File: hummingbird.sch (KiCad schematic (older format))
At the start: 40 parts

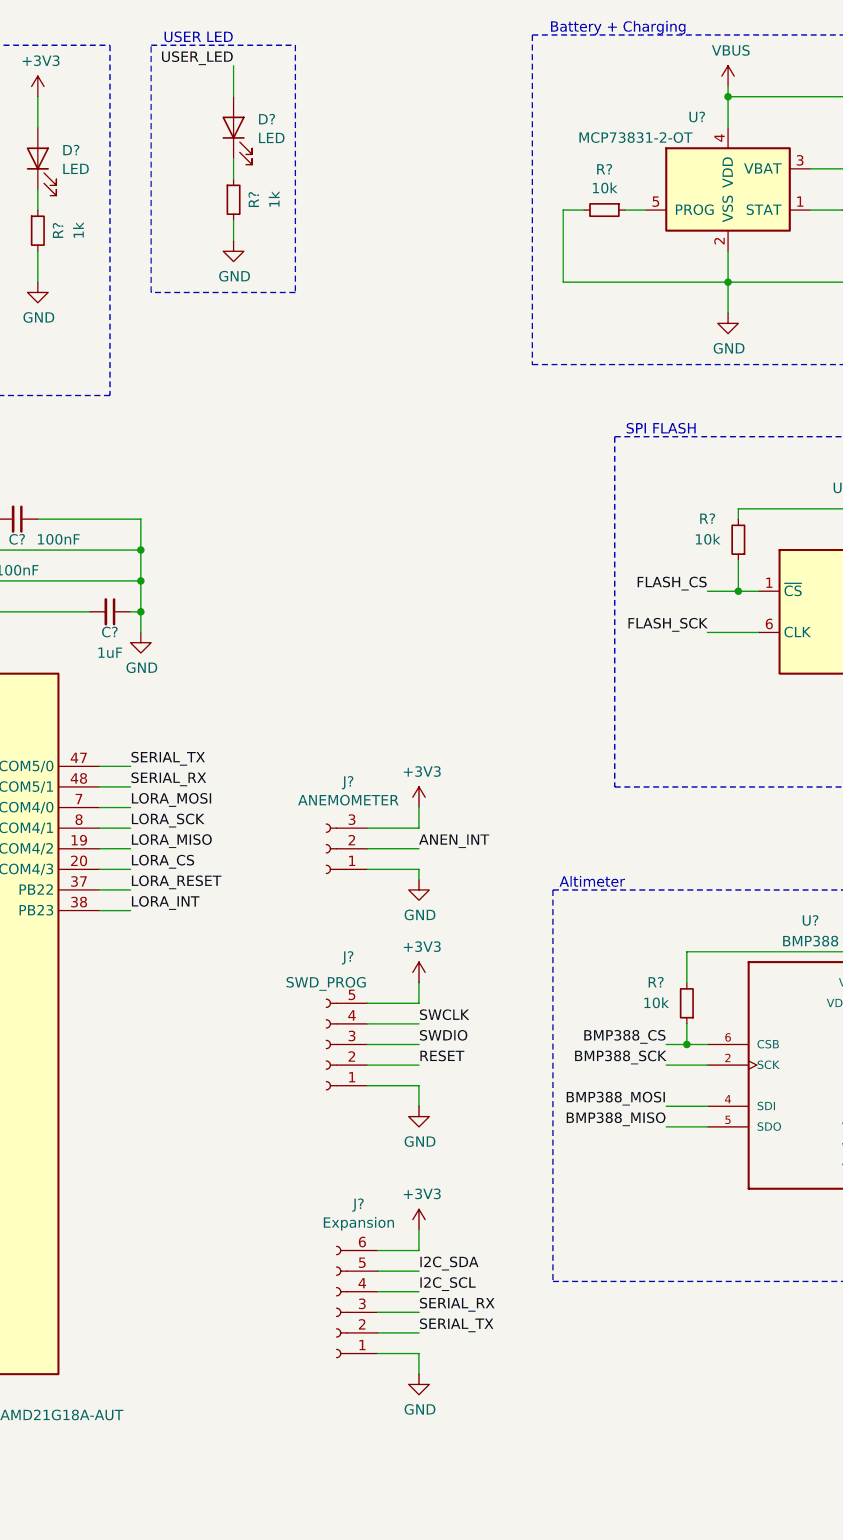
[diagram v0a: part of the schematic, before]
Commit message: renaming things, add SOIC prog clip header
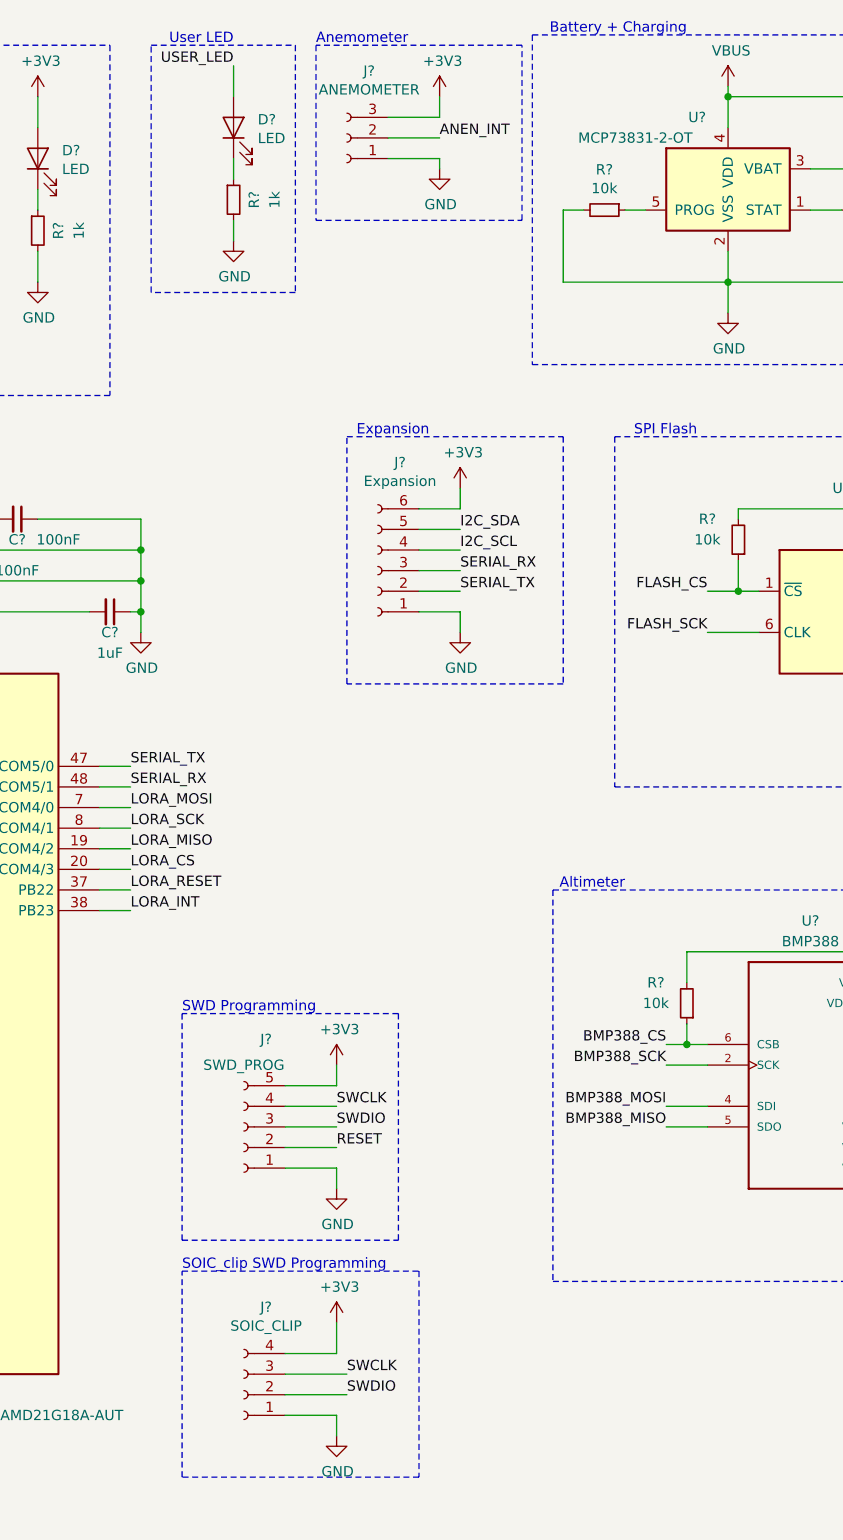
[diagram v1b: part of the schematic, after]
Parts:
- added J?: SOIC_CLIP, symbol Connector:Conn_01x04_Female
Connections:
- net +3V3: now also J?.4 (Pin_4)
- net GND: now also J?.1 (Pin_1)
- net SWCLK: now also J?.3 (Pin_3)
- net SWDIO: now also J?.2 (Pin_2)
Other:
- note added: "Anemometer"
- note added: "Expansion"
- note added: "SOIC_clip SWD Programming"
- note added: "SPI Flash"
- note added: "SWD Programming"
- note added: "User LED"
- note removed: "SPI FLASH"
- note removed: "USER LED"
- moved on the sheet: J?

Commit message: schematic first draft
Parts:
- added TP?: XOUT32, symbol Connector:TestPoint
- added TP?: XIN32, symbol Connector:TestPoint
- C?: value ?? -> 1uF
- J?: value JSTPH -> JST
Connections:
- net at C?.2, U?.1 (PA00), Y?.2: now also TP?.1
- net at C?.2, U?.2 (PA01), Y?.1: now also TP?.1
- no-connect marks 13 -> 21
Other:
- note added: "MCU"
- note removed: "todo"
- moved on the sheet: C?, D?, J?, R?, U?, Y?

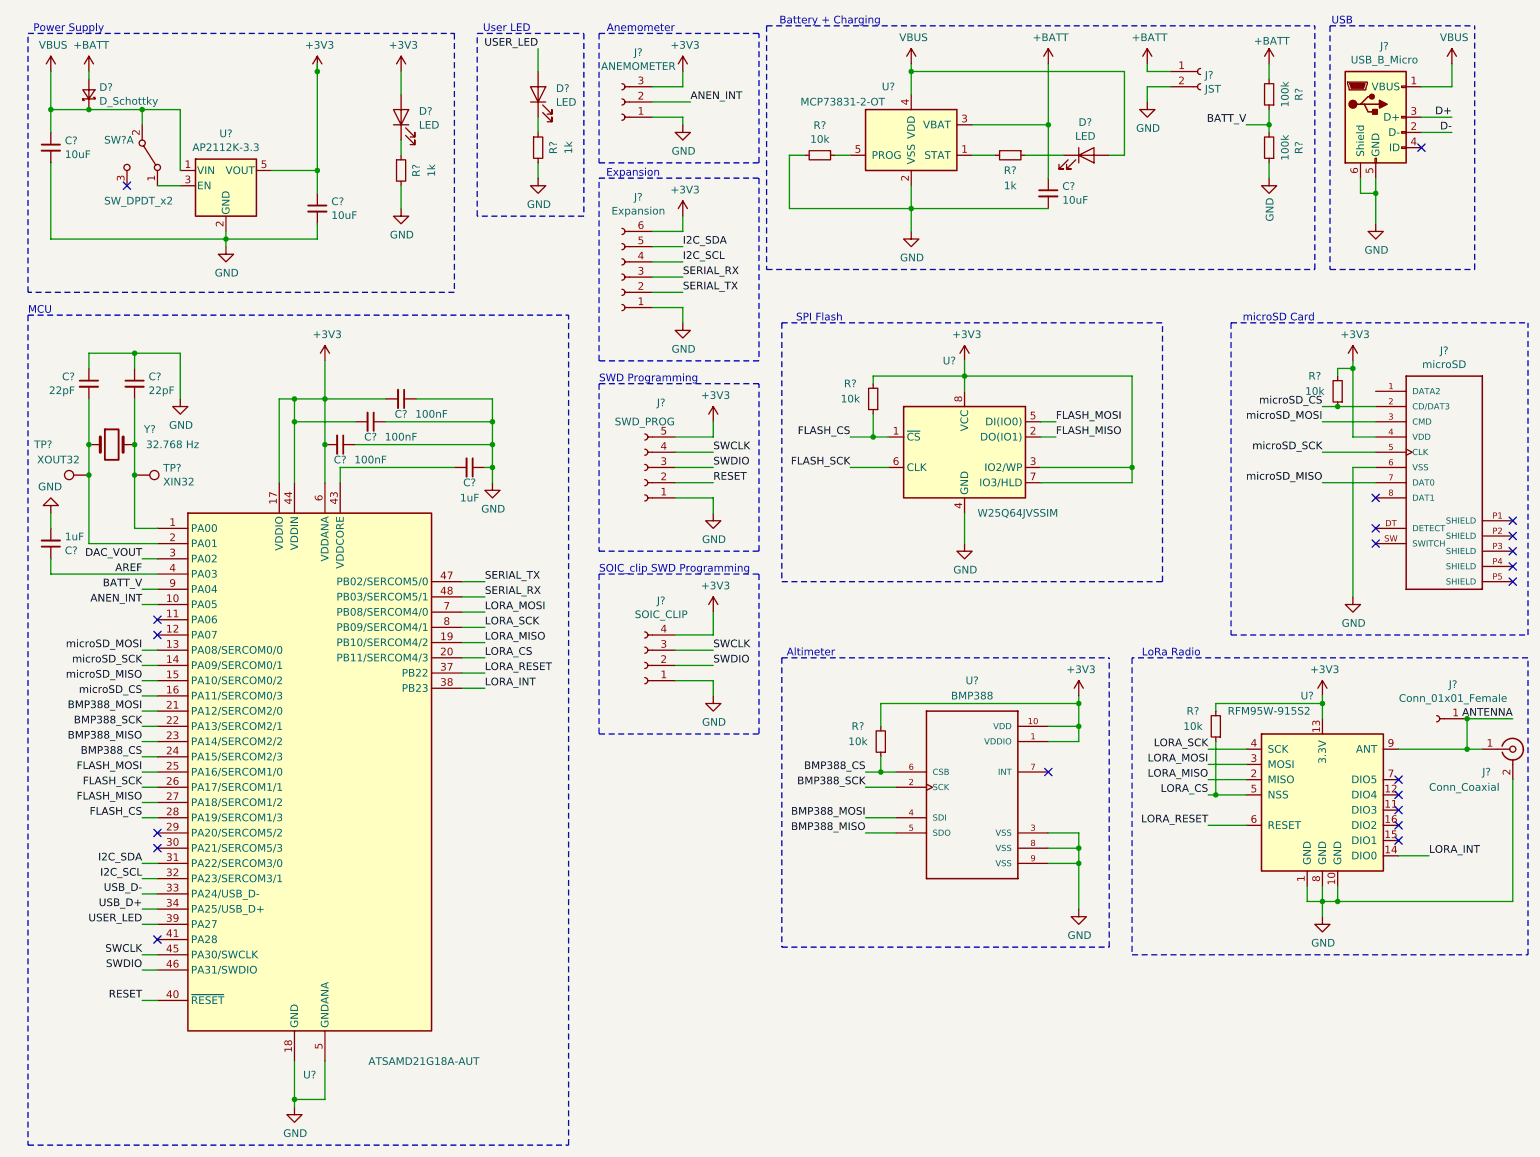
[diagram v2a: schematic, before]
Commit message: actually finish schematic and connect pins
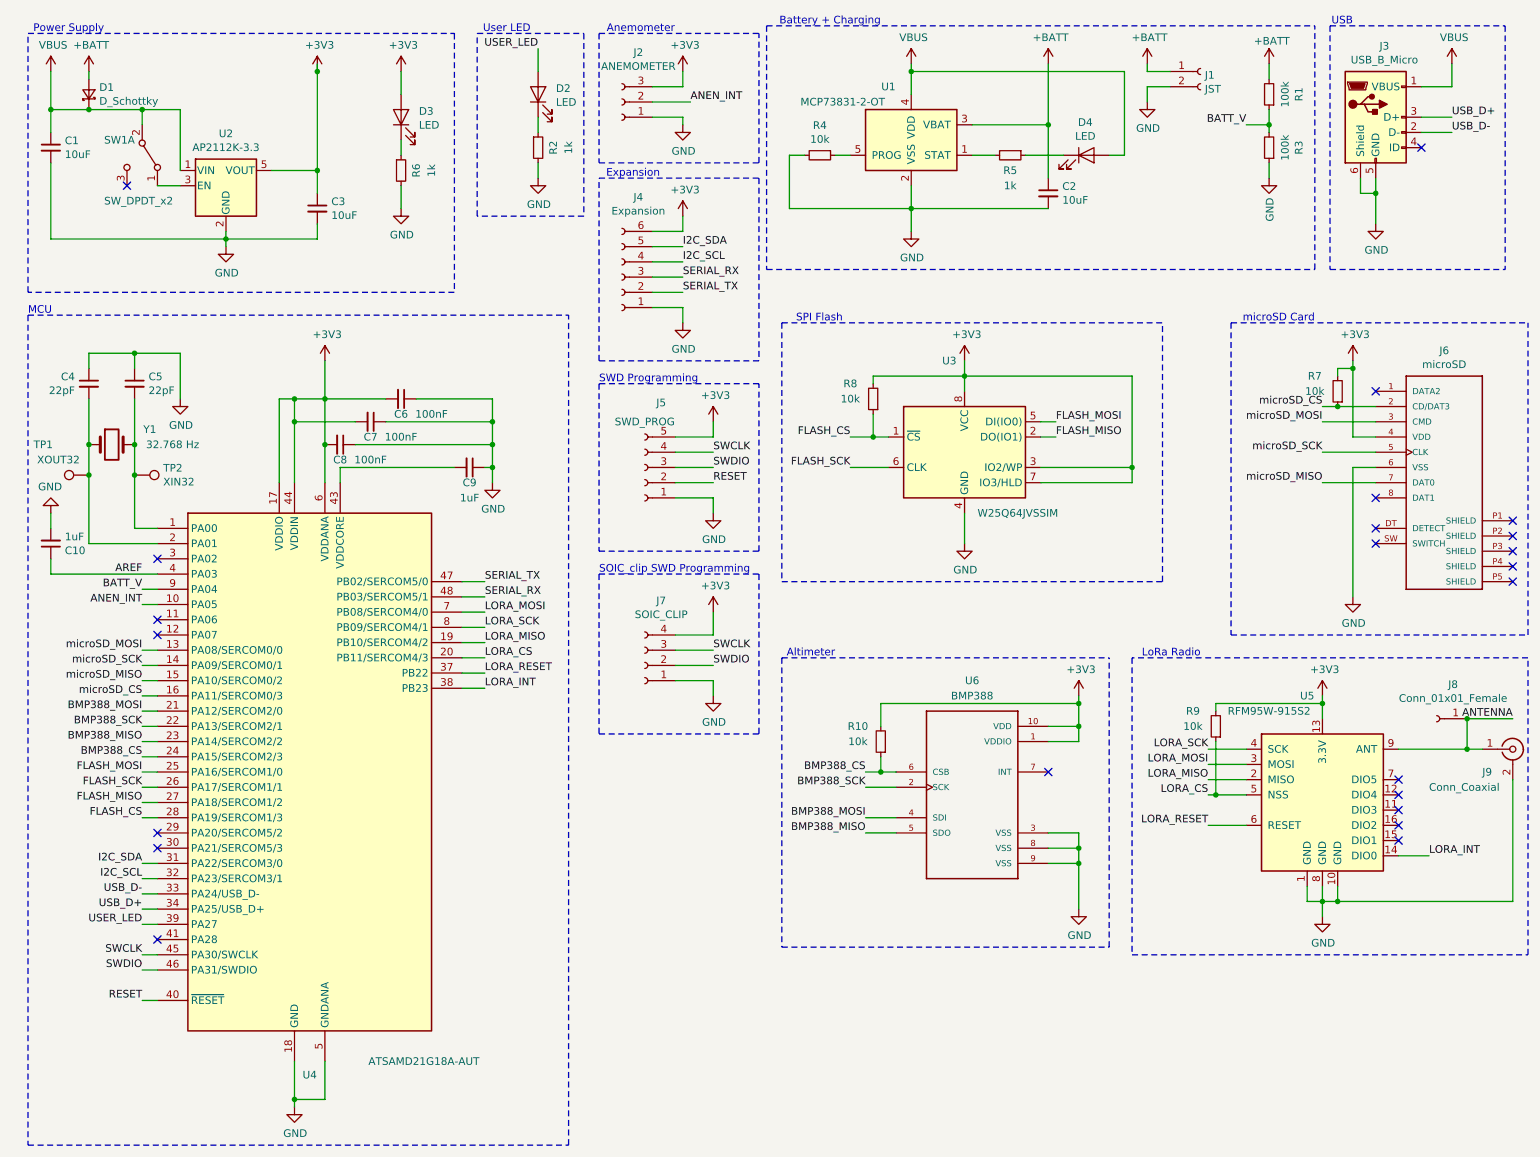
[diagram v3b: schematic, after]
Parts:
- gave numbers to parts that had none: 43
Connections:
- net D+ is gone; now on net USB_D+: J3.3 (D+)
- net D- is gone; now on net USB_D-: J3.2 (D-)
- net DAC_VOUT: no longer names the net of U4.3 (PA02)
- no-connect marks 21 -> 23

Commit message: start adding footprints
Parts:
- C1, C10, C2, C3, C4, C5, C6, C7, C8, C9: footprint (none) -> Capacitor_SMD:C_0603_1608Metric
- D1: footprint (none) -> Diode_SMD:D_0603_1608Metric
- D2, D3, D4: footprint (none) -> LED_SMD:LED_0603_1608Metric
- J2: footprint (none) -> Connector_PinHeader_2.54mm:PinHeader_1x03_P2.54mm_Vertical
- J4: footprint (none) -> Connector_PinHeader_2.54mm:PinHeader_1x06_P2.54mm_Vertical
- J5: footprint (none) -> Connector_PinHeader_2.54mm:PinHeader_1x05_P2.54mm_Vertical
- J6: footprint MOLEX_503182-1852 -> (none)
- J9: footprint (none) -> Connector_Coaxial:SMA_Molex_73251-1153_EdgeMount_Horizontal
- R1, R10, R2, R3, R4, R5, R6, R7, R8, R9: footprint (none) -> Resistor_SMD:R_0603_1608Metric
- TP1, TP2: footprint (none) -> TestPoint:TestPoint_Pad_D1.0mm
- U6: footprint PQFN50P200X200X80-10N -> (none)
- Y1: footprint (none) -> Crystal:Crystal_SMD_3215-2Pin_3.2x1.5mm
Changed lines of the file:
@@
 F 0 "C9" V 3600 3500 50  0000 C CNN
 F 1 "1uF" V 3700 3500 50  0000 C CNN
-F 2 "" H 3500 3500 50  0001 C CNN
+F 2 "Capacitor_SMD:C_0603_1608Metric" H 3500 3500 50  0001 C CNN
 F 3 "~" H 3500 3500 50  0001 C CNN
 	1    3500 3500
@@
 F 0 "C8" V 2750 3350 50  0000 C CNN
 F 1 "100nF" V 2750 3550 50  0000 C CNN
-F 2 "" H 2650 3350 50  0001 C CNN
+F 2 "Capacitor_SMD:C_0603_1608Metric" H 2650 3350 50  0001 C CNN
 F 3 "~" H 2650 3350 50  0001 C CNN
 	1    2650 3350
@@
 F 0 "C7" V 2950 3200 50  0000 C CNN
 F 1 "100nF" V 2950 3400 50  0000 C CNN
-F 2 "" H 2850 3200 50  0001 C CNN
+F 2 "Capacitor_SMD:C_0603_1608Metric" H 2850 3200 50  0001 C CNN
 F 3 "~" H 2850 3200 50  0001 C CNN
 	1    2850 3200
@@
 F 0 "C6" V 3150 3050 50  0000 C CNN
 F 1 "100nF" V 3150 3250 50  0000 C CNN
-F 2 "" H 3050 3050 50  0001 C CNN
+F 2 "Capacitor_SMD:C_0603_1608Metric" H 3050 3050 50  0001 C CNN
 F 3 "~" H 3050 3050 50  0001 C CNN
 	1    3050 3050
@@
 F 0 "C3" H 2592 1846 50  0000 L CNN
 F 1 "10uF" H 2592 1755 50  0000 L CNN
-F 2 "" H 2500 1800 50  0001 C CNN
+F 2 "Capacitor_SMD:C_0603_1608Metric" H 2500 1800 50  0001 C CNN
 F 3 "~" H 2500 1800 50  0001 C CNN
 	1    2500 1800
@@
 F 0 "D1" V 1046 982 50  0000 R CNN
 F 1 "D_Schottky" V 955 982 50  0000 R CNN
-F 2 "" V 1000 1050 50  0001 C CNN
+F 2 "Diode_SMD:D_0603_1608Metric" V 1000 1050 50  0001 C CNN
 F 3 "~" V 1000 1050 50  0001 C CNN
 	1    1000 1050
@@
 F 0 "C1" H 842 1446 50  0000 L CNN
 F 1 "10uF" H 842 1355 50  0000 L CNN
-F 2 "" H 750 1400 50  0001 C CNN
+F 2 "Capacitor_SMD:C_0603_1608Metric" H 750 1400 50  0001 C CNN
 F 3 "~" H 750 1400 50  0001 C CNN
 	1    750  1400
@@
 F 0 "D4" H 7543 1666 50  0000 C CNN
 F 1 "LED" H 7543 1575 50  0000 C CNN
-F 2 "" H 7550 1450 50  0001 C CNN
+F 2 "LED_SMD:LED_0603_1608Metric" H 7550 1450 50  0001 C CNN
 F 3 "~" H 7550 1450 50  0001 C CNN
 	1    7550 1450
@@
 F 0 "R5" V 7150 1450 50  0000 C CNN
 F 1 "1k" V 7250 1450 50  0000 C CNN
-F 2 "" H 7050 1450 50  0001 C CNN
+F 2 "Resistor_SMD:R_0603_1608Metric" H 7050 1450 50  0001 C CNN
 F 3 "~" H 7050 1450 50  0001 C CNN
 	1    7050 1450
@@
 F 0 "C2" H 7392 1746 50  0000 L CNN
 F 1 "10uF" H 7392 1655 50  0000 L CNN
-F 2 "" H 7300 1700 50  0001 C CNN
+F 2 "Capacitor_SMD:C_0603_1608Metric" H 7300 1700 50  0001 C CNN
 F 3 "~" H 7300 1700 50  0001 C CNN
 	1    7300 1700
@@
 F 0 "R4" V 5604 1450 50  0000 C CNN
 F 1 "10k" V 5695 1450 50  0000 C CNN
-F 2 "" H 5800 1450 50  0001 C CNN
+F 2 "Resistor_SMD:R_0603_1608Metric" H 5800 1450 50  0001 C CNN
 F 3 "~" H 5800 1450 50  0001 C CNN
 	1    5800 1450
@@
 F 0 "R1" V 8554 1050 50  0000 C CNN
 F 1 "100k" V 8645 1050 50  0000 C CNN
-F 2 "" H 8750 1050 50  0001 C CNN
+F 2 "Resistor_SMD:R_0603_1608Metric" H 8750 1050 50  0001 C CNN
 F 3 "~" H 8750 1050 50  0001 C CNN
 	1    8750 1050
@@
 F 0 "R3" V 8554 1400 50  0000 C CNN
 F 1 "100k" V 8645 1400 50  0000 C CNN
-F 2 "" H 8750 1400 50  0001 C CNN
+F 2 "Resistor_SMD:R_0603_1608Metric" H 8750 1400 50  0001 C CNN
 F 3 "~" H 8750 1400 50  0001 C CNN
 	1    8750 1400
@@
 F 0 "U6" H 6800 6500 50  0000 C CNN
 F 1 "BMP388" H 6800 6400 50  0000 C CNN
-F 2 "PQFN50P200X200X80-10N" H 6800 5700 50  0001 L BNN
+F 2 "" H 6800 5700 50  0001 L BNN
 F 3 "https://ae-bst.resource.bosch.com/media/_tech/media/datasheets/BST-BMP388-DS001.pdf" H 6800 5700 50  0001 L BNN
 F 4 "828-1079-1-ND" H 6800 5700 50  0001 L BNN "Field4"
@@
 F 0 "J6" H 9900 4467 50  0000 C CNN
 F 1 "microSD" H 9900 4376 50  0000 C CNN
-F 2 "MOLEX_503182-1852" H 10400 3400 50  0001 L BNN
+F 2 "" H 10400 3400 50  0001 L BNN
 F 3 "https://www.molex.com/pdm_docs/sd/5031821852_sd.pdf" H 10350 3750 50  0001 L BNN
 F 4 "MICRO SD NORMAL ULTRALOWPRO8CKTE" H 10350 4050 50  0001 L BNN "Field4"
@@
 F 0 "J9" H 10150 5200 50  0000 L CNN
 F 1 "Conn_Coaxial" H 9800 5100 50  0000 L CNN
-F 2 "" H 10350 5350 50  0001 C CNN
+F 2 "Connector_Coaxial:SMA_Molex_73251-1153_EdgeMount_Horizontal" H 10350 5350 50  0001 C CNN
 F 3 " ~" H 10350 5350 50  0001 C CNN
 	1    10350 5350
@@
 F 0 "D3" V 3089 1083 50  0000 R CNN
 F 1 "LED" V 2998 1083 50  0000 R CNN
-F 2 "" H 3050 1200 50  0001 C CNN
+F 2 "LED_SMD:LED_0603_1608Metric" H 3050 1200 50  0001 C CNN
 F 3 "~" H 3050 1200 50  0001 C CNN
 	1    3050 1200
@@
 F 0 "D2" V 3989 933 50  0000 R CNN
 F 1 "LED" V 3898 933 50  0000 R CNN
-F 2 "" H 3950 1050 50  0001 C CNN
+F 2 "LED_SMD:LED_0603_1608Metric" H 3950 1050 50  0001 C CNN
 F 3 "~" H 3950 1050 50  0001 C CNN
 	1    3950 1050
@@
 F 0 "R6" V 3150 1550 50  0000 C CNN
 F 1 "1k" V 3250 1550 50  0000 C CNN
-F 2 "" H 3050 1550 50  0001 C CNN
+F 2 "Resistor_SMD:R_0603_1608Metric" H 3050 1550 50  0001 C CNN
 F 3 "~" H 3050 1550 50  0001 C CNN
 	1    3050 1550
@@
 F 0 "R2" V 4050 1400 50  0000 C CNN
 F 1 "1k" V 4150 1400 50  0000 C CNN
-F 2 "" H 3950 1400 50  0001 C CNN
+F 2 "Resistor_SMD:R_0603_1608Metric" H 3950 1400 50  0001 C CNN
 F 3 "~" H 3950 1400 50  0001 C CNN
 	1    3950 1400
@@
 F 0 "Y1" H 1400 3450 50  0000 C CNN
 F 1 "32.768 Hz" H 1550 3350 50  0000 C CNN
-F 2 "" H 1150 3350 50  0001 C CNN
+F 2 "Crystal:Crystal_SMD_3215-2Pin_3.2x1.5mm" H 1150 3350 50  0001 C CNN
 F 3 "https://abracon.com/Resonators/ABS07.pdf" H 1150 3350 50  0001 C CNN
 	1    1150 3350
@@
 F 0 "C4" H 1092 2996 50  0000 L CNN
 F 1 "22pF" H 1092 2905 50  0000 L CNN
-F 2 "" H 1000 2950 50  0001 C CNN
+F 2 "Capacitor_SMD:C_0603_1608Metric" H 1000 2950 50  0001 C CNN
 F 3 "~" H 1000 2950 50  0001 C CNN
 	1    1000 2950
@@
 F 0 "C5" H 1392 2996 50  0000 L CNN
 F 1 "22pF" H 1392 2905 50  0000 L CNN
-F 2 "" H 1300 2950 50  0001 C CNN
+F 2 "Capacitor_SMD:C_0603_1608Metric" H 1300 2950 50  0001 C CNN
 F 3 "~" H 1300 2950 50  0001 C CNN
 	1    1300 2950
@@
 F 0 "J5" H 4542 3075 50  0000 C CNN
 F 1 "SWD_PROG" H 4650 3200 50  0000 C CNN
-F 2 "" H 4650 3500 50  0001 C CNN
+F 2 "Connector_PinHeader_2.54mm:PinHeader_1x05_P2.54mm_Vertical" H 4650 3500 50  0001 C CNN
 F 3 "~" H 4650 3500 50  0001 C CNN
 	1    4650 3500
@@
 F 0 "C10" H 842 4046 50  0000 L CNN
 F 1 "1uF" H 842 3955 50  0000 L CNN
-F 2 "" H 750 4000 50  0001 C CNN
+F 2 "Capacitor_SMD:C_0603_1608Metric" H 750 4000 50  0001 C CNN
 F 3 "~" H 750 4000 50  0001 C CNN
 	1    750  4000
@@
 F 0 "J2" H 4392 775 50  0000 C CNN
 F 1 "ANEMOMETER" H 4392 866 50  0000 C CNN
-F 2 "" H 4500 1100 50  0001 C CNN
+F 2 "Connector_PinHeader_2.54mm:PinHeader_1x03_P2.54mm_Vertical" H 4500 1100 50  0001 C CNN
 F 3 "~" H 4500 1100 50  0001 C CNN
 	1    4500 1100
@@
 F 0 "J4" H 4392 1725 50  0000 C CNN
 F 1 "Expansion" H 4392 1816 50  0000 C CNN
-F 2 "" H 4500 2250 50  0001 C CNN
+F 2 "Connector_PinHeader_2.54mm:PinHeader_1x06_P2.54mm_Vertical" H 4500 2250 50  0001 C CNN
 F 3 "~" H 4500 2250 50  0001 C CNN
 	1    4500 2250
@@
 F 0 "R8" H 6300 2950 50  0000 C CNN
 F 1 "10k" H 6300 3050 50  0000 C CNN
-F 2 "" H 6150 3050 50  0001 C CNN
+F 2 "Resistor_SMD:R_0603_1608Metric" H 6150 3050 50  0001 C CNN
 F 3 "~" H 6150 3050 50  0001 C CNN
 	1    6150 3050
@@
 F 0 "R7" H 9350 2900 50  0000 C CNN
 F 1 "10k" H 9350 3000 50  0000 C CNN
-F 2 "" H 9200 3000 50  0001 C CNN
+F 2 "Resistor_SMD:R_0603_1608Metric" H 9200 3000 50  0001 C CNN
 F 3 "~" H 9200 3000 50  0001 C CNN
 	1    9200 3000
@@
 F 0 "R9" H 8550 5100 50  0000 C CNN
 F 1 "10k" H 8550 5200 50  0000 C CNN
-F 2 "" H 8400 5200 50  0001 C CNN
+F 2 "Resistor_SMD:R_0603_1608Metric" H 8400 5200 50  0001 C CNN
 F 3 "~" H 8400 5200 50  0001 C CNN
 	1    8400 5200
@@
 F 0 "R10" H 6350 5200 50  0000 C CNN
 F 1 "10k" H 6350 5300 50  0000 C CNN
-F 2 "" H 6200 5300 50  0001 C CNN
+F 2 "Resistor_SMD:R_0603_1608Metric" H 6200 5300 50  0001 C CNN
 F 3 "~" H 6200 5300 50  0001 C CNN
 	1    6200 5300
@@
 F 0 "TP1" V 1200 3850 50  0000 C CNN
 F 1 "XOUT32" V 1100 3750 50  0000 C CNN
-F 2 "" H 1200 3550 50  0001 C CNN
+F 2 "TestPoint:TestPoint_Pad_D1.0mm" H 1200 3550 50  0001 C CNN
 F 3 "~" H 1200 3550 50  0001 C CNN
 	1    1000 3550
@@
 F 0 "TP2" V 1254 3738 50  0000 L CNN
 F 1 "XIN32" V 1345 3738 50  0000 L CNN
-F 2 "" H 1500 3550 50  0001 C CNN
+F 2 "TestPoint:TestPoint_Pad_D1.0mm" H 1500 3550 50  0001 C CNN
 F 3 "~" H 1500 3550 50  0001 C CNN
 	1    1300 3550
